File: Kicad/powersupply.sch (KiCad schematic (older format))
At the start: 18 parts, among them J801 Jack-DC, Q801 BC546, Q802 BC556, U801 DC-DC Module, U802 MAX1615, U803 TLV1117 3.3V 1A

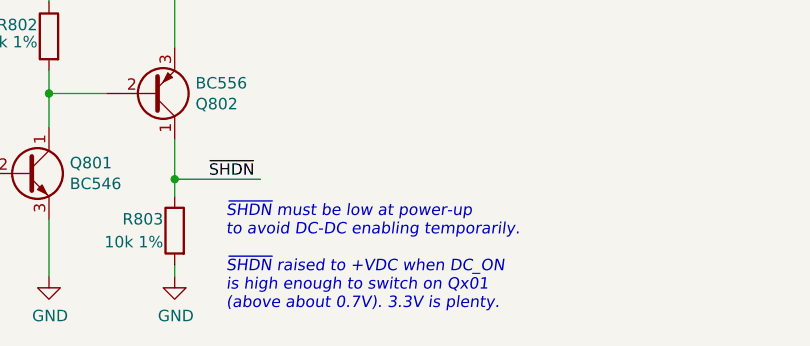
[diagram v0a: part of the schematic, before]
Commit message: Tidy-ups.
) Rewired audio block to pico
) Clarified meaning of USB power jumper and gave better
warning about not plugging in power when jumper fitted.
) We can refer to components now our sheet numbers don't change - note
Q801 on powersupply sheet
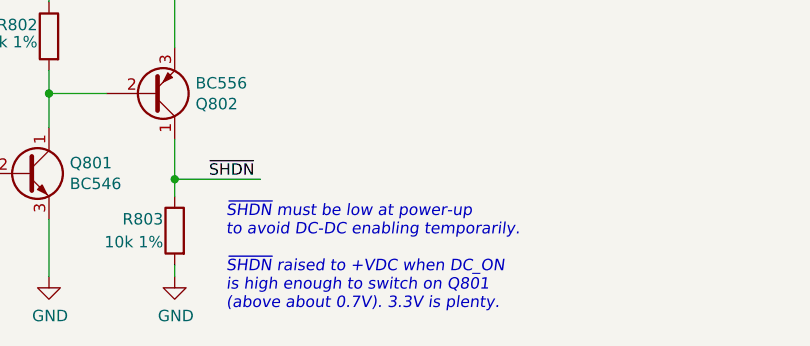
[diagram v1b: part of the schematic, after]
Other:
- note added: "~SHDN~ must be low at power-up\nto avoid DC-DC enabling temporarily.\n\n~SHDN~ raised to +VDC when DC_ON\nis high enough to switch on Q801\n(above about 0.7V). 3.3V is plenty."
- note removed: "~SHDN~ must be low at power-up\nto avoid DC-DC enabling temporarily.\n\n~SHDN~ raised to +VDC when DC_ON\nis high enough to switch on Qx01\n(above about 0.7V). 3.3V is plenty."
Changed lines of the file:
@@
 $EndComp
 Text Notes 2800 6500 0    50   Italic 0
-~SHDN~ must be low at power-up\nto avoid DC-DC enabling temporarily.\n\n~SHDN~ raised to +VDC when DC_ON\nis high enough to switch on Qx01\n(above about 0.7V). 3.3V is plenty.
+~SHDN~ must be low at power-up\nto avoid DC-DC enabling temporarily.\n\n~SHDN~ raised to +VDC when DC_ON\nis high enough to switch on Q801\n(above about 0.7V). 3.3V is plenty.
 $Comp
 L Device:R R802

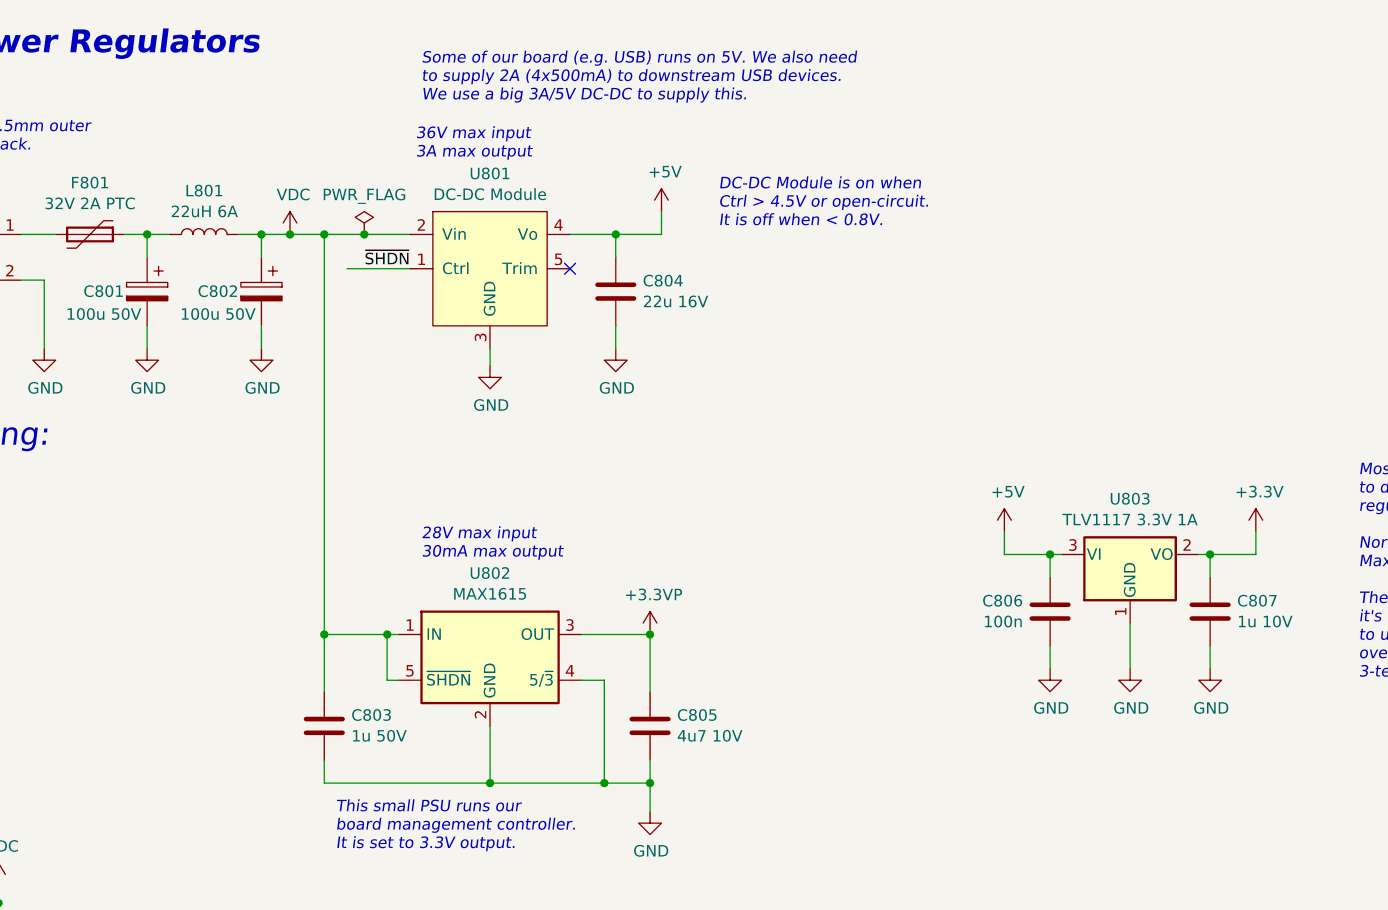
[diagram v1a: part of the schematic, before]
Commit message: Switching some parts over to the CPL.
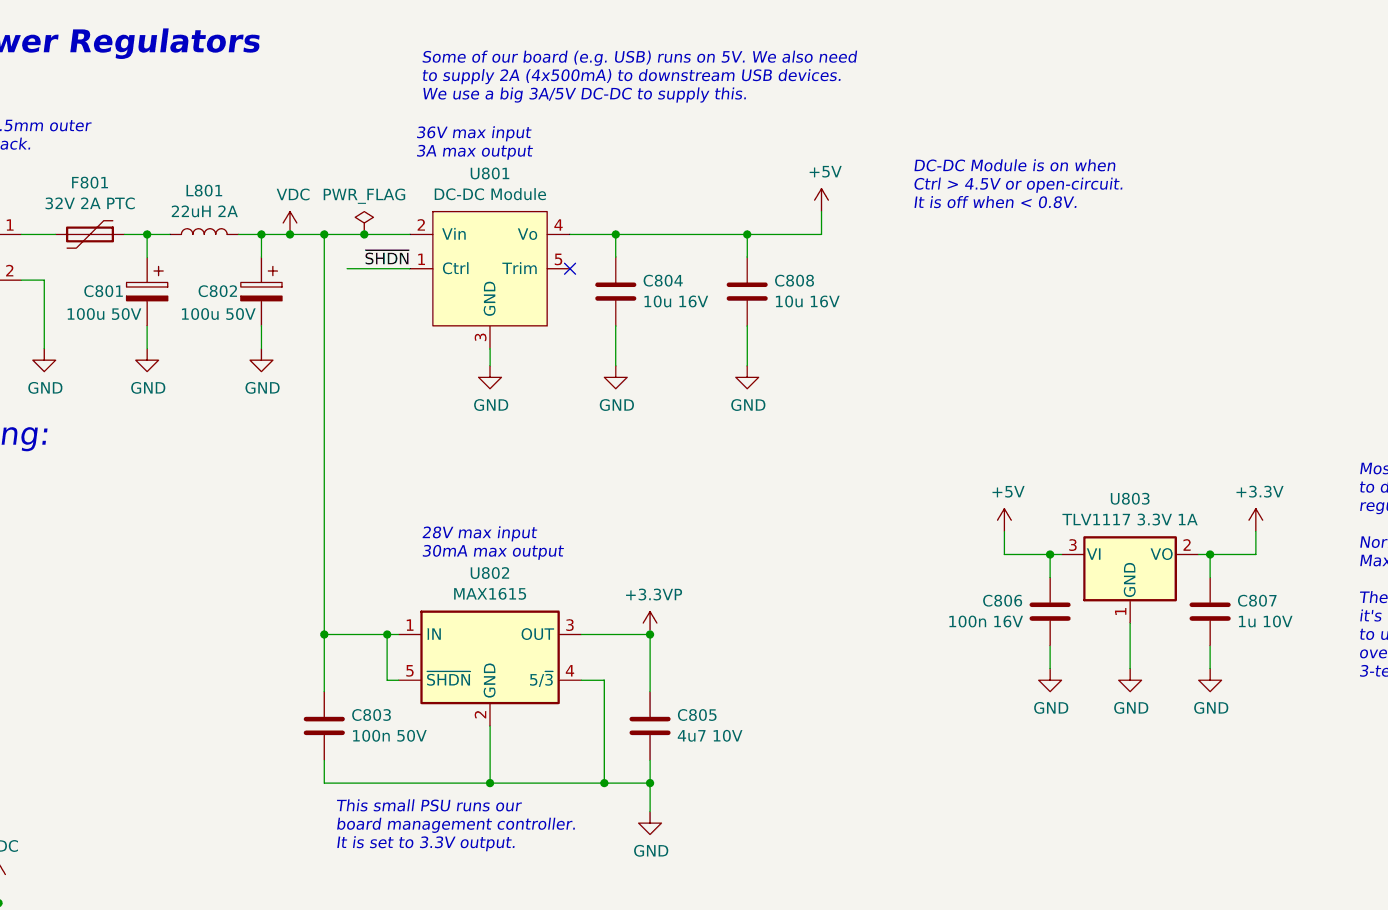
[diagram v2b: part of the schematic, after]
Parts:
- added C808: 10u 16V, Capacitor_SMD:C_0805_2012Metric_Pad1.18x1.45mm_HandSolder, symbol Device:C
- C801, C802: Digikey 493-5916-1-ND -> (none); MPN UVR1H101MPD1TD -> CPL-CAP-ALU-RAD-100UF-50V; Manufacturer Nichicon -> CPL; Mouser 647-UVR1H101MPD1TD -> (none)
- C803: value 1u 50V -> 100n 50V; Digikey 1276-6470-1-ND -> (none); MPN CL21B105KBFNNNG -> CPL-CAP-X7R-0805-100NF-50V; Manufacturer Samsung -> CPL
- C804: value 22u 16V -> 10u 16V; Digikey 1276-7092-1-ND -> (none); MPN CL21A226KOQNNNG -> CPL-CAP-X5R-0805-10UF-16V; Manufacturer Samsung -> CPL
- C805: Digikey 1276-6464-1-ND -> (none); MPN CL21A475KPFNNNG -> CPL-CAP-X5R-0805-4.7UF-25V; Manufacturer Samsung -> CPL
- C806: value 100n -> 100n 16V; Digikey BC1150CT-ND -> (none); MPN K104K15X7RF5TL2 -> CPL-CAP-X7R-0805-100NF-50V; Manufacturer Vishay -> CPL; Mouser 594-K104K15X7RF5TL2 -> (none)
- C807: Digikey 1276-6471-1-ND -> (none); MPN CL21B105KOFNNNG -> CPL-CAP-X7R-0805-1UF-25V; Manufacturer Samsung -> CPL
- L801: value 22uH 6A -> 22uH 2A; footprint Inductor_THT:L_Axial_L26.7mm_D12.1mm_P35.00mm_Horizontal_Vishay_IHA-103 -> Inductor_THT:L_Radial_D9.5mm_P5.00mm_Fastron_07HVP; Digikey AIAP-03-220K-ND -> 811-2042-ND; MPN AIAP-03-220K -> 13R223C; Manufacturer Abracon -> Murata; Mouser 815-AIAP03220K -> (none)
- Q801, Q802: DNP (none) -> 0
- R801, R802, R803: Digikey RMCF0805FT10K0-ND -> (none); MPN RMCF0805FT10K0 -> CPL-RES-0805-10K-0.125W; Manufacturer Stackpole -> CPL
- U803: MPN TLV1117LV33DCYR -> CPL-REG-LIN-3.3V-1A; Manufacturer Texas Instruments -> CPL
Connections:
- wire segments 63 -> 66
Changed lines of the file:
@@
 F 4 "0" H 7525 3525 50  0001 C CNN "DNP"
 F 5 "296-28778-1-ND" H 7525 3525 50  0001 C CNN "Digikey"
-F 6 "TLV1117LV33DCYR" H 7525 3525 50  0001 C CNN "MPN"
-F 7 "Texas Instruments" H 7525 3525 50  0001 C CNN "Manufacturer"
+F 6 "CPL-REG-LIN-3.3V-1A" H 7525 3525 50  0001 C CNN "MPN"
+F 7 "CPL" H 7525 3525 50  0001 C CNN "Manufacturer"
 F 8 "595-TLV1117LV33DCYR" H 7525 3525 50  0001 C CNN "Mouser"
 	1    7525 3525
@@
 F 3 "~" H 7875 3775 50  0001 C CNN
 F 4 "0" H 7875 3775 50  0001 C CNN "DNP"
-F 5 "1276-6471-1-ND" H 7875 3775 50  0001 C CNN "Digikey"
-F 6 "CL21B105KOFNNNG" H 7875 3775 50  0001 C CNN "MPN"
-F 7 "Samsung" H 7875 3775 50  0001 C CNN "Manufacturer"
+F 5 "" H 7875 3775 50  0001 C CNN "Digikey"
+F 6 "CPL-CAP-X7R-0805-1UF-25V" H 7875 3775 50  0001 C CNN "MPN"
+F 7 "CPL" H 7875 3775 50  0001 C CNN "Manufacturer"
 	1    7875 3775
 	1    0    0    -1
@@
 P 4000 4275
 F 0 "C803" H 4118 4321 50  0000 L CNN
-F 1 "1u 50V" H 4118 4230 50  0000 L CNN
+F 1 "100n 50V" H 4118 4230 50  0000 L CNN
 F 2 "Capacitor_SMD:C_0805_2012Metric_Pad1.18x1.45mm_HandSolder" H 4038 4125 50  0001 C CNN
 F 3 "~" H 4000 4275 50  0001 C CNN
 F 4 "0" H 4000 4275 50  0001 C CNN "DNP"
-F 5 "1276-6470-1-ND" H 4000 4275 50  0001 C CNN "Digikey"
-F 6 "CL21B105KBFNNNG" H 4000 4275 50  0001 C CNN "MPN"
-F 7 "Samsung" H 4000 4275 50  0001 C CNN "Manufacturer"
+F 5 "" H 4000 4275 50  0001 C CNN "Digikey"
+F 6 "CPL-CAP-X7R-0805-100NF-50V" H 4000 4275 50  0001 C CNN "MPN"
+F 7 "CPL" H 4000 4275 50  0001 C CNN "Manufacturer"
 	1    4000 4275
 	1    0    0    -1
@@
 L power:+5V #PWR0812
 U 1 1 606E29D8
-P 5475 2025
-F 0 "#PWR0812" H 5475 1875 50  0001 C CNN
-F 1 "+5V" H 5490 2198 50  0000 C CNN
-F 2 "" H 5475 2025 50  0001 C CNN
-F 3 "" H 5475 2025 50  0001 C CNN
-	1    5475 2025
+P 6175 2025
+F 0 "#PWR0812" H 6175 1875 50  0001 C CNN
+F 1 "+5V" H 6190 2198 50  0000 C CNN
+F 2 "" H 6175 2025 50  0001 C CNN
+F 3 "" H 6175 2025 50  0001 C CNN
+	1    6175 2025
 	1    0    0    -1
 $EndComp
@@
 P 7175 3775
 F 0 "C806" H 7293 3821 50  0000 L CNN
-F 1 "100n" H 7293 3730 50  0000 L CNN
+F 1 "100n 16V" H 7293 3730 50  0000 L CNN
 F 2 "Capacitor_SMD:C_0805_2012Metric_Pad1.18x1.45mm_HandSolder" H 7213 3625 50  0001 C CNN
 F 3 "~" H 7175 3775 50  0001 C CNN
 F 4 "0" H 7175 3775 50  0001 C CNN "DNP"
-F 5 "BC1150CT-ND" H 7175 3775 50  0001 C CNN "Digikey"
-F 6 "K104K15X7RF5TL2" H 7175 3775 50  0001 C CNN "MPN"
-F 7 "Vishay" H 7175 3775 50  0001 C CNN "Manufacturer"
-F 8 "594-K104K15X7RF5TL2" H 7175 3775 50  0001 C CNN "Mouser"
+F 5 "" H 7175 3775 50  0001 C CNN "Digikey"
+F 6 "CPL-CAP-X7R-0805-100NF-50V" H 7175 3775 50  0001 C CNN "MPN"
+F 7 "CPL" H 7175 3775 50  0001 C CNN "Manufacturer"
+F 8 "" H 7175 3775 50  0001 C CNN "Mouser"
 	1    7175 3775
 	-1   0    0    -1
@@
 L power:GND #PWR0809
 U 1 1 606E29DA
-P 5275 2625
-F 0 "#PWR0809" H 5275 2375 50  0001 C CNN
-F 1 "GND" H 5280 2452 50  0000 C CNN
-F 2 "" H 5275 2625 50  0001 C CNN
-F 3 "" H 5275 2625 50  0001 C CNN
-	1    5275 2625
+P 5275 2700
+F 0 "#PWR0809" H 5275 2450 50  0001 C CNN
+F 1 "GND" H 5280 2527 50  0000 C CNN
+F 2 "" H 5275 2700 50  0001 C CNN
+F 3 "" H 5275 2700 50  0001 C CNN
+	1    5275 2700
 	1    0    0    -1
 $EndComp
@@
 P 5275 2375
 F 0 "C804" H 5393 2421 50  0000 L CNN
-F 1 "22u 16V" H 5393 2330 50  0000 L CNN
+F 1 "10u 16V" H 5393 2330 50  0000 L CNN
 F 2 "Capacitor_SMD:C_0805_2012Metric_Pad1.18x1.45mm_HandSolder" H 5313 2225 50  0001 C CNN
 F 3 "~" H 5275 2375 50  0001 C CNN
 F 4 "0" H 5275 2375 50  0001 C CNN "DNP"
-F 5 "1276-7092-1-ND" H 5275 2375 50  0001 C CNN "Digikey"
-F 6 "CL21A226KOQNNNG" H 5275 2375 50  0001 C CNN "MPN"
-F 7 "Samsung" H 5275 2375 50  0001 C CNN "Manufacturer"
+F 5 "" H 5275 2375 50  0001 C CNN "Digikey"
+F 6 "CPL-CAP-X5R-0805-10UF-16V" H 5275 2375 50  0001 C CNN "MPN"
+F 7 "CPL" H 5275 2375 50  0001 C CNN "Manufacturer"
 	1    5275 2375
 	1    0    0    -1
@@
 P 3475 2125
 F 0 "L801" V 3665 2125 50  0000 C CNN
-F 1 "22uH 6A" V 3574 2125 50  0000 C CNN
-F 2 "Inductor_THT:L_Axial_L26.7mm_D12.1mm_P35.00mm_Horizontal_Vishay_IHA-103" H 3475 2125 50  0001 C CNN
-F 3 "https://abracon.com/Magnetics/axial/AIAP-03.pdf" H 3475 2125 50  0001 C CNN
+F 1 "22uH 2A" V 3574 2125 50  0000 C CNN
+F 2 "Inductor_THT:L_Radial_D9.5mm_P5.00mm_Fastron_07HVP" H 3475 2125 50  0001 C CNN
+F 3 "https://www.murata-ps.com/pub/data/magnetics/kmp_1300r.pdf" H 3475 2125 50  0001 C CNN
 F 4 "0" H 3475 2125 50  0001 C CNN "DNP"
-F 5 "AIAP-03-220K" V 3475 2125 50  0001 C CNN "MPN"
-F 6 "Abracon" V 3475 2125 50  0001 C CNN "Manufacturer"
-F 7 "AIAP-03-220K-ND" V 3475 2125 50  0001 C CNN "Digikey"
-F 8 "815-AIAP03220K" H 3475 2125 50  0001 C CNN "Mouser"
+F 5 "13R223C" V 3475 2125 50  0001 C CNN "MPN"
+F 6 "Murata" V 3475 2125 50  0001 C CNN "Manufacturer"
+F 7 "811-2042-ND" V 3475 2125 50  0001 C CNN "Digikey"
+F 8 "" H 3475 2125 50  0001 C CNN "Mouser"
 	1    3475 2125
 	0    -1   -1   0
@@
 F 3 "~" H 3225 2375 50  0001 C CNN
 F 4 "0" H 3225 2375 50  0001 C CNN "DNP"
-F 5 "493-5916-1-ND" H 3225 2375 50  0001 C CNN "Digikey"
-F 6 "UVR1H101MPD1TD" H 3225 2375 50  0001 C CNN "MPN"
-F 7 "Nichicon" H 3225 2375 50  0001 C CNN "Manufacturer"
-F 8 "647-UVR1H101MPD1TD" H 3225 2375 50  0001 C CNN "Mouser"
+F 5 "" H 3225 2375 50  0001 C CNN "Digikey"
+F 6 "CPL-CAP-ALU-RAD-100UF-50V" H 3225 2375 50  0001 C CNN "MPN"
+F 7 "CPL" H 3225 2375 50  0001 C CNN "Manufacturer"
+F 8 "" H 3225 2375 50  0001 C CNN "Mouser"
 	1    3225 2375
 	-1   0    0    -1
@@
 F 3 "~" H 3725 2375 50  0001 C CNN
 F 4 "0" H 3725 2375 50  0001 C CNN "DNP"
-F 5 "493-5916-1-ND" H 3725 2375 50  0001 C CNN "Digikey"
-F 6 "UVR1H101MPD1TD" H 3725 2375 50  0001 C CNN "MPN"
-F 7 "Nichicon" H 3725 2375 50  0001 C CNN "Manufacturer"
-F 8 "647-UVR1H101MPD1TD" H 3725 2375 50  0001 C CNN "Mouser"
+F 5 "" H 3725 2375 50  0001 C CNN "Digikey"
+F 6 "CPL-CAP-ALU-RAD-100UF-50V" H 3725 2375 50  0001 C CNN "MPN"
+F 7 "CPL" H 3725 2375 50  0001 C CNN "Manufacturer"
+F 8 "" H 3725 2375 50  0001 C CNN "Mouser"
 	1    3725 2375
 	-1   0    0    -1
@@
 	8075 3525 7875 3525
 Wire Wire Line
-	5275 2625 5275 2525
+	5275 2700 5275 2525
 Wire Wire Line
 	5275 2225 5275 2125
@@
 	7525 4025 7525 3825
 Wire Wire Line
-	5275 2125 5475 2125
+	5275 2125 5850 2125
 Wire Wire Line
 	7175 3625 7175 3525
@@
 F 3 "~" H 5425 4275 50  0001 C CNN
 F 4 "0" H 5425 4275 50  0001 C CNN "DNP"
-F 5 "1276-6464-1-ND" H 5425 4275 50  0001 C CNN "Digikey"
-F 6 "CL21A475KPFNNNG" H 5425 4275 50  0001 C CNN "MPN"
-F 7 "Samsung" H 5425 4275 50  0001 C CNN "Manufacturer"
+F 5 "" H 5425 4275 50  0001 C CNN "Digikey"
+F 6 "CPL-CAP-X5R-0805-4.7UF-25V" H 5425 4275 50  0001 C CNN "MPN"
+F 7 "CPL" H 5425 4275 50  0001 C CNN "Manufacturer"
 	1    5425 4275
 	1    0    0    -1
@@
 Connection ~ 5425 4525
 Wire Wire Line
-	5475 2025 5475 2125
+	6175 2025 6175 2125
 $Comp
 L power:+5V #PWR0813
@@
 Text HLabel 1325 5900 0    50   Input ~ 0
 DC_ON
-Text Notes 5725 2100 0    50   Italic 0
+Text Notes 6575 2025 0    50   Italic 0
 DC-DC Module is on when\nCtrl > 4.5V or open-circuit.\nIt is off when < 0.8V.
 Wire Wire Line
@@
 F 5 "BC546CTA" H 1925 5900 50  0001 C CNN "MPN"
 F 6 "ON Semiconductor" H 1925 5900 50  0001 C CNN "Manufacturer"
+F 7 "0" H 1925 5900 50  0001 C CNN "DNP"
 	1    1925 5900
 	1    0    0    -1
@@
 F 5 "BC556BTFCT-ND" H 2475 5550 50  0001 C CNN "Digikey"
 F 6 "ON Semiconductor" H 2475 5550 50  0001 C CNN "Manufacturer"
+F 7 "0" H 2475 5550 50  0001 C CNN "DNP"
 	1    2475 5550
 	1    0    0    1
@@
 F 3 "~" H 1550 5900 50  0001 C CNN
 F 4 "0" H 1550 5900 50  0001 C CNN "DNP"
-F 5 "RMCF0805FT10K0-ND" H 1550 5900 50  0001 C CNN "Digikey"
-F 6 "RMCF0805FT10K0" H 1550 5900 50  0001 C CNN "MPN"
-F 7 "Stackpole" H 1550 5900 50  0001 C CNN "Manufacturer"
+F 5 "" H 1550 5900 50  0001 C CNN "Digikey"
+F 6 "CPL-RES-0805-10K-0.125W" H 1550 5900 50  0001 C CNN "MPN"
+F 7 "CPL" H 1550 5900 50  0001 C CNN "Manufacturer"
 	1    1550 5900
 	0    1    -1   0
@@
 F 3 "~" H 2025 5300 50  0001 C CNN
 F 4 "0" H 2025 5300 50  0001 C CNN "DNP"
-F 5 "RMCF0805FT10K0-ND" H 2025 5300 50  0001 C CNN "Digikey"
-F 6 "RMCF0805FT10K0" H 2025 5300 50  0001 C CNN "MPN"
-F 7 "Stackpole" H 2025 5300 50  0001 C CNN "Manufacturer"
+F 5 "" H 2025 5300 50  0001 C CNN "Digikey"
+F 6 "CPL-RES-0805-10K-0.125W" H 2025 5300 50  0001 C CNN "MPN"
+F 7 "CPL" H 2025 5300 50  0001 C CNN "Manufacturer"
 	1    2025 5300
 	-1   0    0    -1
@@
 F 3 "~" H 2575 6150 50  0001 C CNN
 F 4 "0" H 2575 6150 50  0001 C CNN "DNP"
-F 5 "RMCF0805FT10K0-ND" H 2575 6150 50  0001 C CNN "Digikey"
-F 6 "RMCF0805FT10K0" H 2575 6150 50  0001 C CNN "MPN"
-F 7 "Stackpole" H 2575 6150 50  0001 C CNN "Manufacturer"
+F 5 "" H 2575 6150 50  0001 C CNN "Digikey"
+F 6 "CPL-RES-0805-10K-0.125W" H 2575 6150 50  0001 C CNN "MPN"
+F 7 "CPL" H 2575 6150 50  0001 C CNN "Manufacturer"
 	1    2575 6150
 	-1   0    0    -1
@@
 	1    0    0    -1
 $EndComp
+$Comp
+L Device:C C808
+U 1 1 60E7E52A
+P 5850 2375
+F 0 "C808" H 5968 2421 50  0000 L CNN
+F 1 "10u 16V" H 5968 2330 50  0000 L CNN
+F 2 "Capacitor_SMD:C_0805_2012Metric_Pad1.18x1.45mm_HandSolder" H 5888 2225 50  0001 C CNN
+F 3 "~" H 5850 2375 50  0001 C CNN
+F 4 "0" H 5850 2375 50  0001 C CNN "DNP"
+F 5 "" H 5850 2375 50  0001 C CNN "Digikey"
+F 6 "CPL-CAP-X5R-0805-10UF-16V" H 5850 2375 50  0001 C CNN "MPN"
+F 7 "CPL" H 5850 2375 50  0001 C CNN "Manufacturer"
+	1    5850 2375
+	1    0    0    -1
+$EndComp
+$Comp
+L power:GND #PWR01
+U 1 1 60E86C1C
+P 5850 2700
+F 0 "#PWR01" H 5850 2450 50  0001 C CNN
+F 1 "GND" H 5855 2527 50  0000 C CNN
+F 2 "" H 5850 2700 50  0001 C CNN
+F 3 "" H 5850 2700 50  0001 C CNN
+	1    5850 2700
+	1    0    0    -1
+$EndComp
+Wire Wire Line
+	5850 2700 5850 2525
+Wire Wire Line
+	5850 2225 5850 2125
+Connection ~ 5850 2125
+Wire Wire Line
+	5850 2125 6175 2125
 $EndSCHEMATC
